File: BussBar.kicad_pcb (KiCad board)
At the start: 2 copper layers, 175 x 22 mm, 12 parts, among them J1 INPUT POWER, J2 Conn_02x05_Odd_Even, J3 Conn_02x05_Odd_Even, J4 Conn_02x05_Odd_Even, J5 Conn_02x05_Odd_Even, J6 Conn_02x05_Odd_Even, J7 Conn_02x05_Odd_Even

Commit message: Standof and FP Started
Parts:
- added REF**: MountingHole_3.2mm_M3_DIN965_Pad, MountingHole:MountingHole_3.2mm_M3_DIN965_Pad, F.Cu at (249.9, 148.8)
- added REF**: MountingHole_3.2mm_M3_DIN965_Pad, MountingHole:MountingHole_3.2mm_M3_DIN965_Pad, F.Cu at (181.1, 146.1)

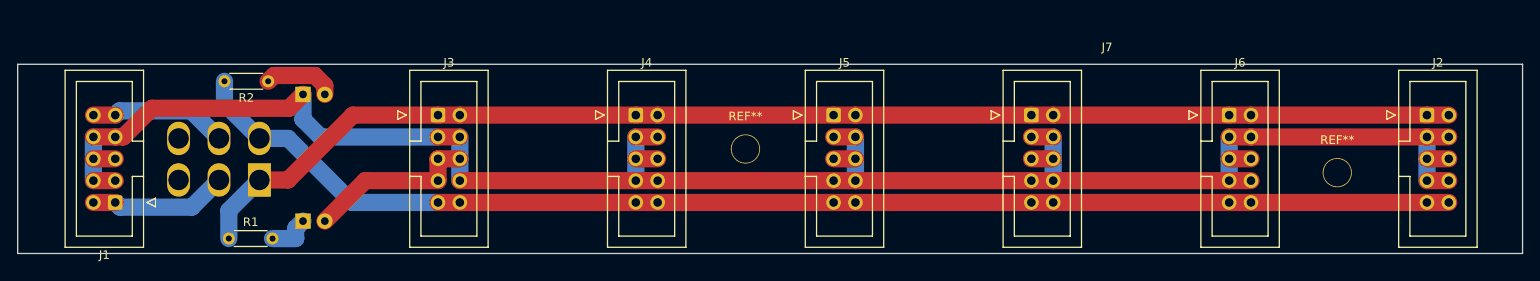
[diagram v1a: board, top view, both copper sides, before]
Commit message: New Mounting Holes
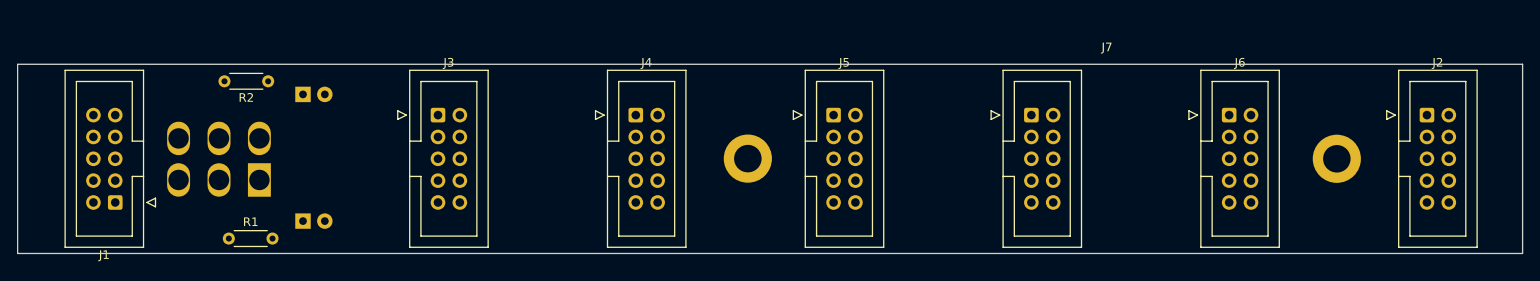
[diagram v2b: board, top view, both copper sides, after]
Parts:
- removed REF** (x2): MountingHole_3.2mm_M3_DIN965_Pad, MountingHole:MountingHole_3.2mm_M3_DIN965_Pad
- added H1: MountingHole_Pad, MountingHole:MountingHole_3.2mm_M3_DIN965_Pad, F.Cu at (181.3, 147.2)
- added H1: MountingHole_Pad, MountingHole:MountingHole_3.2mm_M3_DIN965_Pad, F.Cu at (249.8, 147.2)
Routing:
- net GND: track 249.6 -> 0.00 mm
- net +12s: track 149.8 -> 0.00 mm
- net -12s: track 149.7 -> 0.00 mm
- net +12: track 16.1 -> 0.00 mm
- net -12: track 16.1 -> 0.00 mm
- net Net-(D2-Pad2): track 8.39 -> 0.00 mm
- net Net-(D1-Pad1): track 5.08 -> 0.00 mm

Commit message: Board/FP ready
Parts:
- added GIJO: LOGO, ROBSLIBRARY:Girl7, F.Cu at (229.6, 146.7)
- added GIJO1: LOGO, ROBSLIBRARY:Girl7, B.Cu at (230.2, 147.3)
- renumbered H1 to H2
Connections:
- H1 pad 1: (no net) -> GND
- H2 pad 1: (no net) -> GND
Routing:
- net +12s: track 0.00 -> 151.0 mm
- net -12s: track 0.00 -> 147.9 mm
- net -12: track 0.00 -> 15.8 mm
- net +12: track 0.00 -> 15.7 mm
- net Net-(D2-Pad2): track 0.00 -> 7.89 mm
- net Net-(D1-Pad1): track 0.00 -> 5.03 mm
- added copper zone on B.Cu, net GND
- added copper zone on F.Cu, net GND
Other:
- board text added: "Big Red Buss- PCB V 0.1.0"
- board text added: "CLAYTUNE Big Red Buss By TwinTurbo V0.1.0"
- board text added: "For Kate"
- board text added: "JLCJLCJLCJLC"
- board text removed: "PCB V 0.0.1"
